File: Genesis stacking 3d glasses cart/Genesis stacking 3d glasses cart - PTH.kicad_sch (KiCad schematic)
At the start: 29 parts, among them CON1 GENESIS-EDGE, J1 Conn_01x32_Male, J2 Conn_01x32_Male, J3 top slot connector, J4 3D Glasses, SW1 Pause, U1 74HC133, U2 74HC86, U3 74HC259, U4 LM324

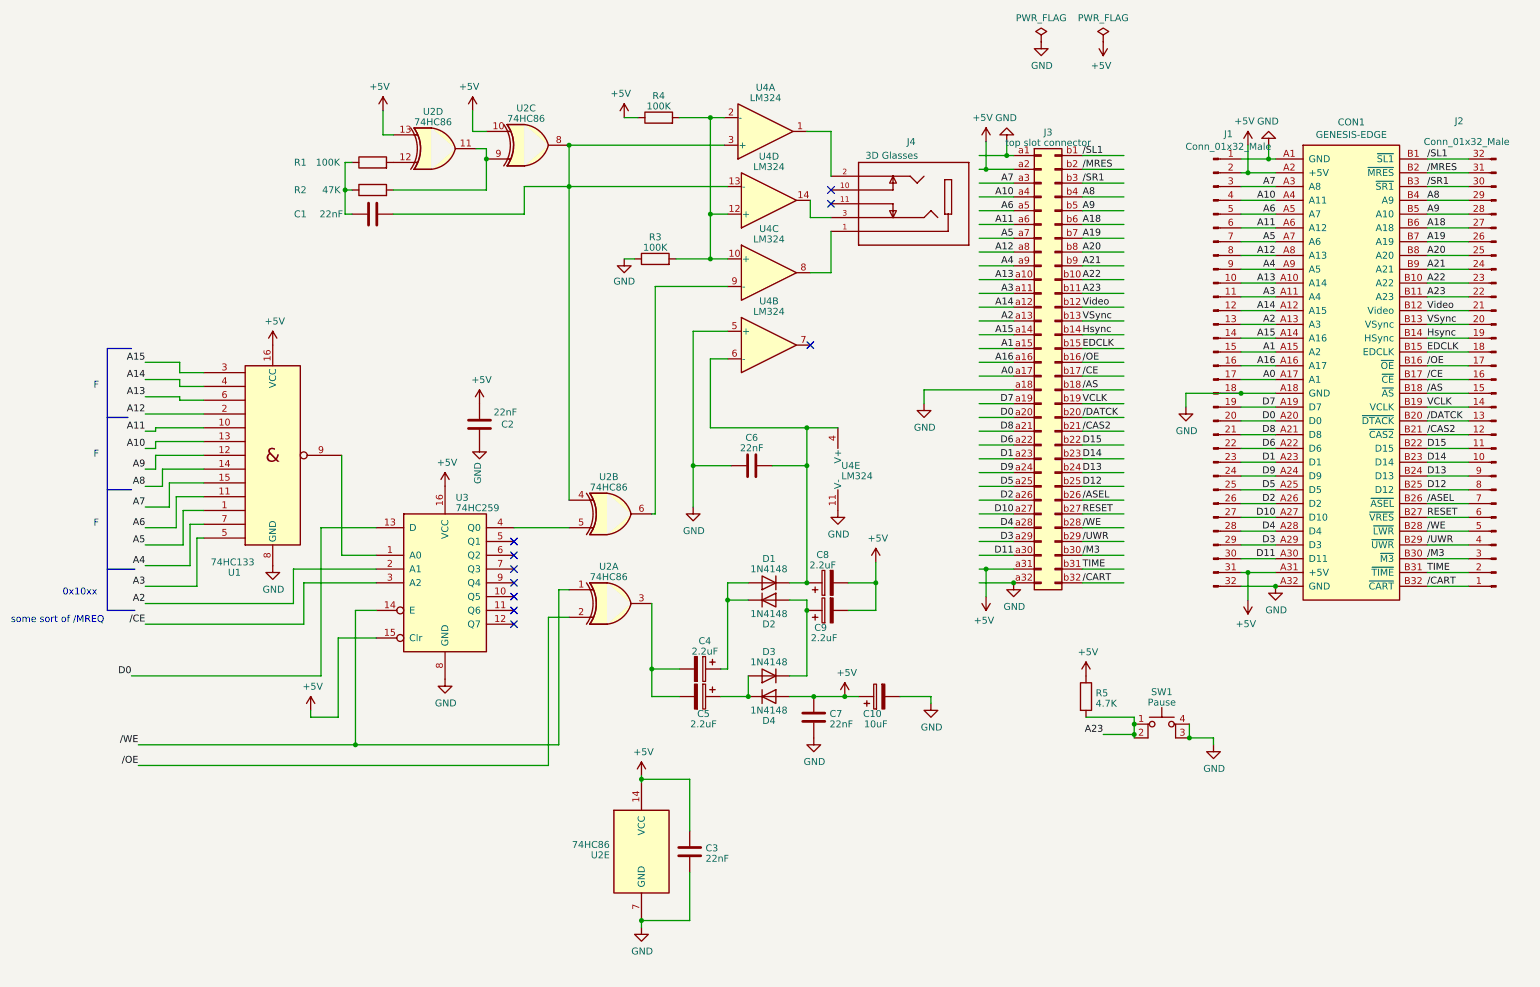
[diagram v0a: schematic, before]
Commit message: added PTH version based on the incorrect schematic and the mostly SMD version based on the reverse engineered board someone made and tested.
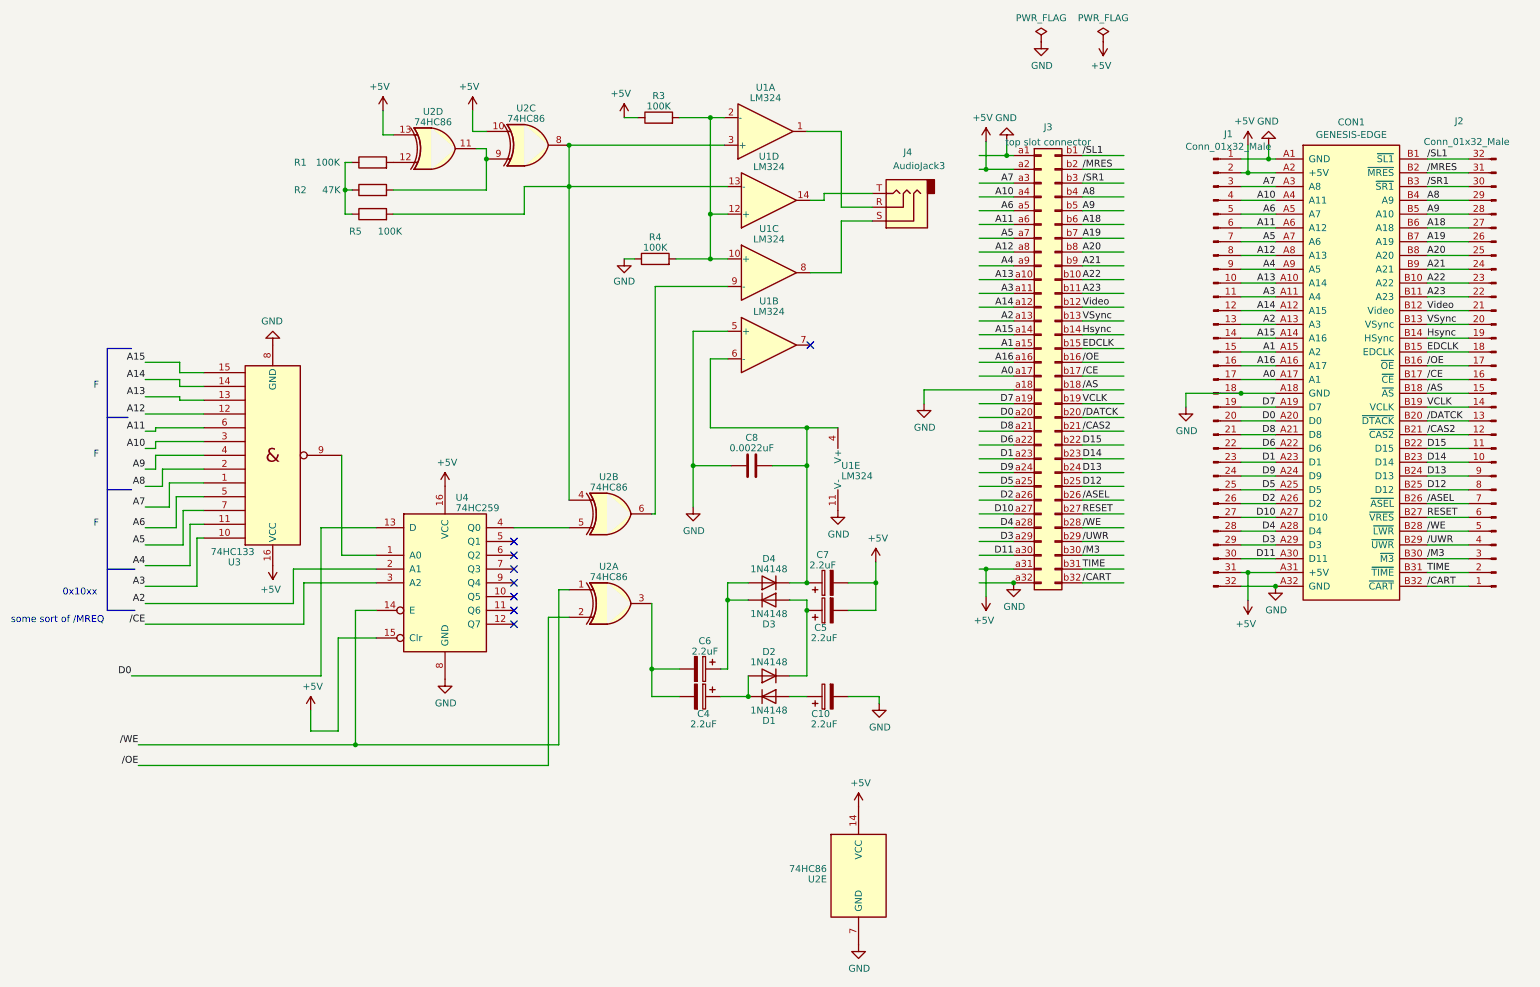
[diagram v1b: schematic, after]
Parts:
- removed C1, C2, C3, C7: 22nF, Capacitor_SMD:C_0603_1608Metric, symbol Device:C
- removed J4: 3D Glasses, Evan's misc parts:CUI_SJ1-3525N, symbol Evan's misc parts:SJ1-3525N
- removed SW1: Pause, Button_Switch_SMD:SW_SPST_Omron_B3FS-105xP, symbol Switch:SW_MEC_5E
- added J4: AudioJack3, Connector_Audio:Jack_3.5mm_CUI_SJ1-3523N_Horizontal, symbol Connector_Audio:AudioJack3
- C10: value 10uF -> 2.2uF
- C8: renamed from C6; value 22nF -> 0.0022uF; footprint Capacitor_SMD:C_0603_1608Metric -> Capacitor_THT:C_Disc_D4.3mm_W1.9mm_P5.00mm
- D1: renamed from D4; footprint Diode_SMD:D_SOD-123F -> Diode_THT:D_DO-35_SOD27_P7.62mm_Horizontal
- D2: renamed from D3; footprint Diode_SMD:D_SOD-123F -> Diode_THT:D_DO-35_SOD27_P7.62mm_Horizontal
- D3: renamed from D2; footprint Diode_SMD:D_SOD-123F -> Diode_THT:D_DO-35_SOD27_P7.62mm_Horizontal
- D4: renamed from D1; footprint Diode_SMD:D_SOD-123F -> Diode_THT:D_DO-35_SOD27_P7.62mm_Horizontal
- R1, R2: footprint Resistor_SMD:R_0603_1608Metric -> Resistor_THT:R_Axial_DIN0204_L3.6mm_D1.6mm_P7.62mm_Horizontal
- R3: renamed from R4; footprint Resistor_SMD:R_0603_1608Metric -> Resistor_THT:R_Axial_DIN0207_L6.3mm_D2.5mm_P2.54mm_Vertical
- R4: renamed from R3; footprint Resistor_SMD:R_0603_1608Metric -> Resistor_THT:R_Axial_DIN0207_L6.3mm_D2.5mm_P2.54mm_Vertical
- R5: value 4.7K -> 100K; footprint Resistor_SMD:R_0603_1608Metric -> Resistor_THT:R_Axial_DIN0204_L3.6mm_D1.6mm_P7.62mm_Horizontal
- U1: renamed from U4; footprint Package_SO:SOIC-14_3.9x8.7mm_P1.27mm -> Package_DIP:DIP-14_W7.62mm
- U2: footprint Package_SO:SOIC-14_3.9x8.7mm_P1.27mm -> Package_DIP:DIP-14_W7.62mm
- U3: renamed from U1; footprint Package_SO:SOIC-16_3.9x9.9mm_P1.27mm -> Package_DIP:DIP-16_W7.62mm
- U4: renamed from U3; footprint Package_SO:SOIC-16_3.9x9.9mm_P1.27mm -> Package_DIP:DIP-16_W7.62mm
- renumbered C5 to C4, C9 to C5, C4 to C6, C8 to C7
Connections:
- net +5V: no longer C10.1, D1.2 (A), R5.1
- net A10: now also U3.3; no longer U3.13
- net A11: now also U3.6; no longer U3.10
- net A12: now also U3.12; no longer U3.2
- net A13: now also U3.13; no longer U3.6
- net A14: now also U3.14; no longer U3.4
- net A15: now also U3.15; no longer U3.3
- net A23: no longer R5.2
- net A3: now also U3.10; no longer U3.5
- net A4: now also U3.11; no longer U3.7
- net A5: now also U3.7; no longer U3.1
- net A6: now also U3.5; no longer U3.11
- net A7: now also U3.1; no longer U3.15
- net A8: now also U3.2; no longer U3.14
- net A9: now also U3.4; no longer U3.12
- net at U1.8: now also J4.S
- net at U1.1: now also J4.R
- net at U1.14: now also J4.T
- net at U1.13 (-), U1.3 (+), U2.4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: now also R5.2
- net at R1.1, R2.1: now also R5.1
- new net: C10.1, D1.2 (A)
- no-connect marks 10 -> 8
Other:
- moved on the sheet: C10, U2E
